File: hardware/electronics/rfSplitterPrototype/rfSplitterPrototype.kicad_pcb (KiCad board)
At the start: 4 copper layers, 40 x 40 mm, 43 parts, among them J1 PRPC002SBAN-M71RC, U1 TPS7A16A-Q1, U2 PMA2-162LNA+, U3 QCN-19D+

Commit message: worked on RF splitter
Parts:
- removed J1: PRPC002SBAN-M71RC, lib_fp:conn_01x02_254_right_angle
- added C10: 100pF, lib_fp:GCM0402, F.Cu at (141.0, 92.6)
- added C11: 100nF, lib_fp:GCM0402, F.Cu at (141.0, 93.8)
- added C13: 470pF, lib_fp:GCM0402, F.Cu at (142.2, 90.0)
- added J2: VAL, lib_fp:conn_01x03_254_right_angle, F.Cu at (153.7, 100.0)
- added L2: 68nH, lib_fp:L_0402, F.Cu at (140.5, 90.5)
- added NT1: NetTie, lib_fp:NetTie-2_SMD_Pad1.0mm, F.Cu at (131.2, 97.0)
- added TP12: ~, lib_fp:TP_2mm, F.Cu at (144.1, 92.6)
- TP9: value RCWCTE -> ~; footprint lib_fp:TP_RCW -> lib_fp:TP_2mm
- moved TP1 9.86 mm to (141.0, 106.4), turned to 0 degrees
- moved TP9 5.94 mm to (140.5, 87.2), turned to 0 degrees
- moved C14 3.35 mm to (144.3, 90.0)
- moved TP6 3.35 mm to (143.8, 87.2)
- moved TP7 3.30 mm to (146.3, 87.2)
- moved C12 3.10 mm to (151.1, 91.5)
- moved C15 3.10 mm to (156.0, 90.0)
- moved C16 3.10 mm to (146.6, 92.2)
- moved C7 3.10 mm to (155.9, 92.4)
- moved C8 3.10 mm to (155.9, 93.8)
- moved C9 3.10 mm to (153.5, 93.8)
- moved L1 3.10 mm to (154.0, 90.5)
- moved L3 3.10 mm to (146.1, 90.5)
- moved R4 3.10 mm to (153.5, 92.4)
- moved R5 3.10 mm to (152.5, 90.5)
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- renumbered C10 to C12, C11 to C14, C12 to C15, C13 to C16, L2 to L3, TP2 to TP1, TP1 to TP2
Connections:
- C14 pad 1: /GNSS_RF-IN -> Net-(C13-Pad2)
- TP6 pad 1: /GNSS_RF-IN -> Net-(C13-Pad2)
- TP9 pad 1: /LNA_RF-GND -> /GNSS_RF-IN
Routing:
- net +3V3: track 0.00 -> 55.5 mm, vias 0 -> 1
- net Net-(C13-Pad2): track 0.00 -> 3.90 mm
- net /RF-SPLIT_SUM: track 4.27 -> 6.17 mm
- net /LNA_RF-OUT: track 7.30 -> 9.08 mm
- net /GNSS_RF-IN: track 8.30 -> 9.55 mm
- net VSS: vias 9 -> 11
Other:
- board text added: "+3V3"
- board text added: "3V3"
- board text added: "5V0"
- board text added: "C14"
- board text removed: "+5V0"
- board text removed: "RF-GND"

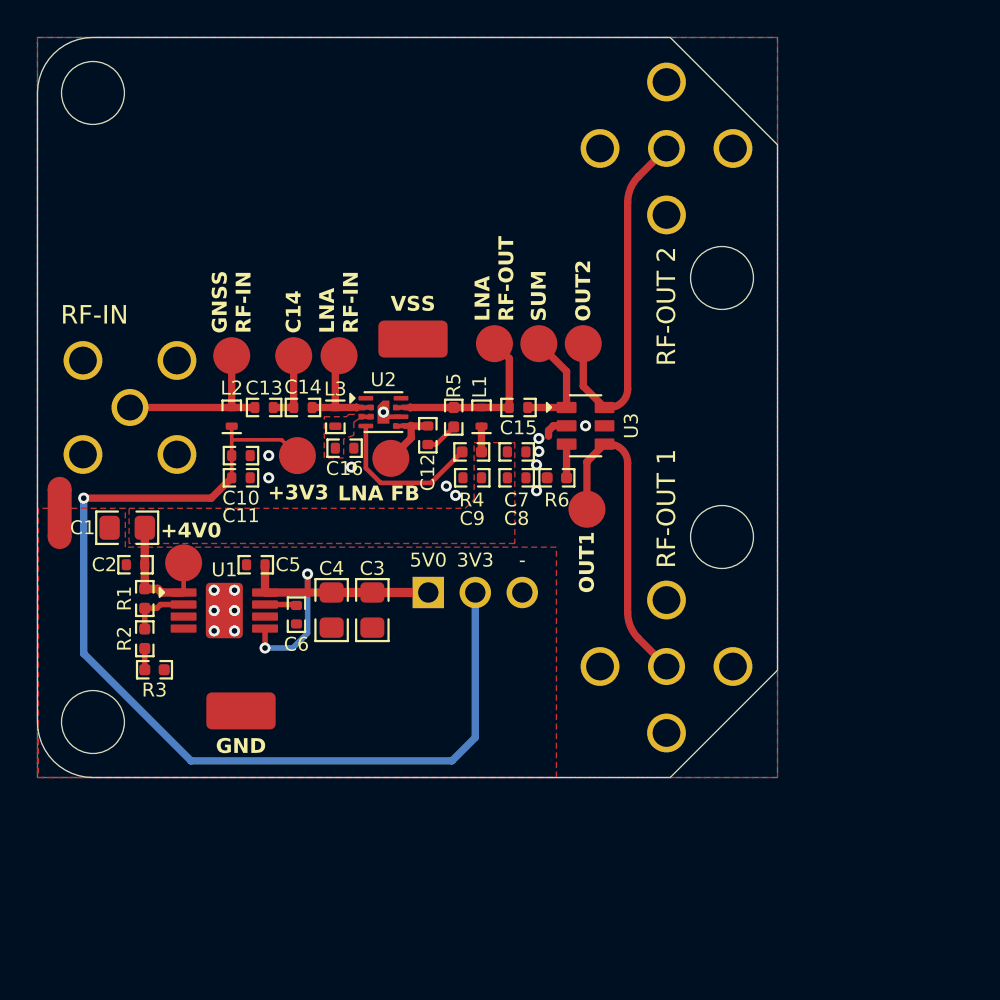
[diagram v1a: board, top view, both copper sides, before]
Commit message: updated with new LNA
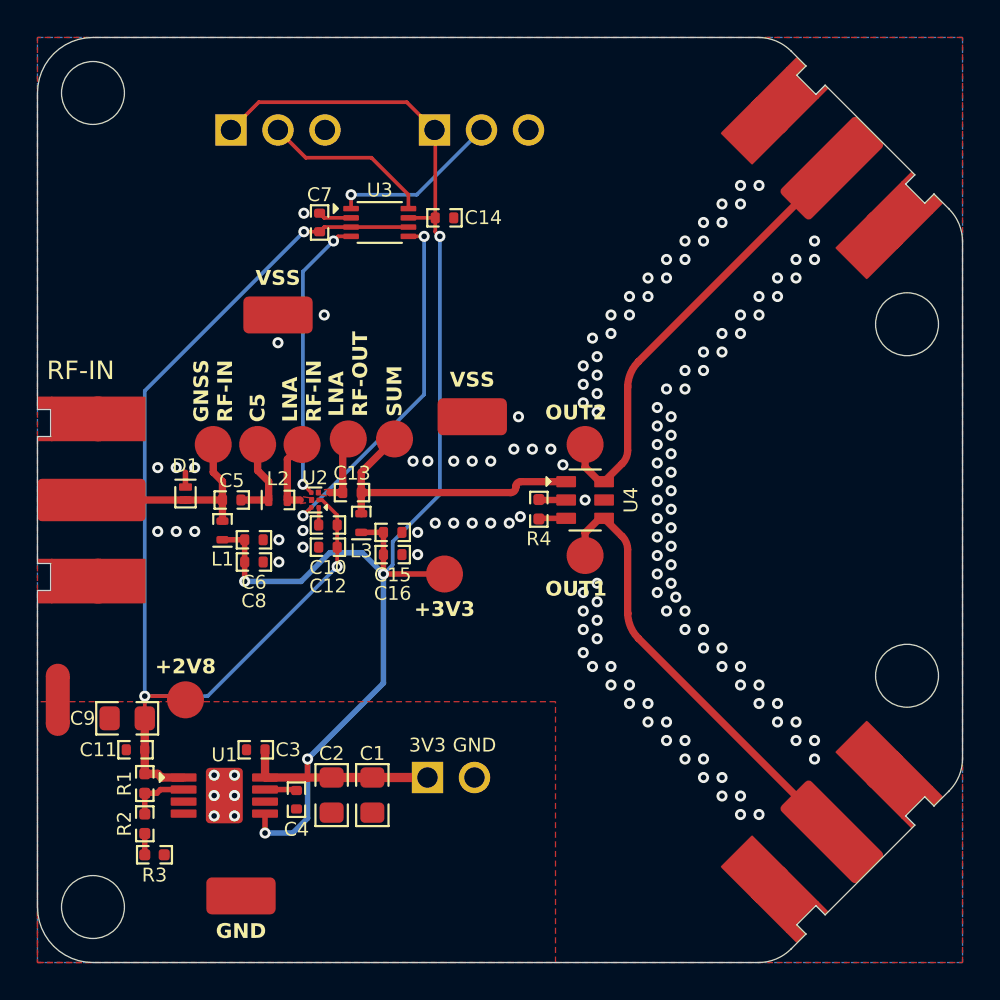
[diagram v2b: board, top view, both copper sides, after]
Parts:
- removed the C8 at (155.9, 93.8)
- removed the C9 at (153.5, 93.8)
- removed the L1 at (154.0, 90.5)
- removed the R4 at (153.5, 92.4)
- removed R5: 267R, lib_fp:CRCW0402
- removed the TP2 at (137.9, 98.4)
- removed the TP3 at (149.1, 92.8)
- removed the TP4 at (154.7, 86.5)
- removed the TP7 at (146.3, 87.2)
- removed the TP8 at (157.1, 86.5)
- added C10: 68pF, lib_fp:GCM0402, F.Cu at (145.7, 96.3)
- added C13: 470pF, lib_fp:GCM0402, F.Cu at (147.0, 94.6)
- added D1: PTVS4V5D1BLYL, lib_fp:SOD882, F.Cu at (138.0, 94.7)
- added J1: VAL, lib_fp:conn_01x02_254_right_angle, F.Cu at (152.3, 110.0)
- added J3: VAL, lib_fp:conn_01x03_254, F.Cu at (154.0, 75.0)
- added L2: 11nH, lib_fp:L_0402, F.Cu at (143.0, 95.0)
- added TP11: RCWCTE, lib_fp:TP_RCW, F.Cu at (143.0, 85.0)
- added TP12: ~, lib_fp:TP_2mm, F.Cu at (138.0, 105.8)
- added TP5: ~, lib_fp:TP_2mm, F.Cu at (144.3, 92.0)
- added TP6: ~, lib_fp:TP_2mm, F.Cu at (149.3, 91.7)
- added TP9: ~, lib_fp:TP_2mm, F.Cu at (146.8, 91.7)
- added U3: TXS0102-Q1, lib_fp:VSSOP50P310X90-8, F.Cu at (148.5, 80.0)
- AE1, AE2, AE3: footprint lib_fp:CONSMA002-G -> lib_fp:0732511153
- C12: value 5.6pF -> 100nF
- C14: value 9.1pF -> 100nF
- C16: value 100pF -> 100nF
- J2: footprint lib_fp:conn_01x03_254_right_angle -> lib_fp:conn_01x03_254
- L3: value 6.8nH -> 68nH
- R1: value 340K -> 220K
- R4: renamed from R6; value 49R9 -> 50R
- U2: value PMA2-162LNA+ -> BGA525N6; footprint lib_fp:TFDFN200X200X100-8 -> lib_fp:XDFN110X70X37-6
- moved J2 27.2 mm to (143.0, 75.0)
- moved C7 16.3 mm to (145.2, 80.0), turned to 90 degrees
- moved AE2 15.6 mm to (175.0, 115.0), turned to 45 degrees
- moved C14 12.8 mm to (152.0, 79.8)
- moved MH4 12.5 mm to (177.0, 104.5)
- moved AE3 11.0 mm to (175.0, 75.0), turned to 135 degrees
- moved MH2 10.3 mm to (177.0, 85.5)
- moved C9 10.3 mm to (134.8, 106.8)
- moved TP3 10.2 mm to (152.0, 99.0)
- moved NT1 10.1 mm to (131.1, 107.1)
- moved C1 10.0 mm to (148.1, 111.0)
- moved C11 10.0 mm to (135.3, 108.5)
- moved C2 10.0 mm to (145.9, 111.0)
- moved C3 10.0 mm to (141.8, 108.5)
- moved C4 10.0 mm to (144.0, 111.2)
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- renumbered C3 to C1, C2 to C11, C4 to C2, C5 to C3, C6 to C4, C13 to C5, C10 to C6, C11 to C8, C1 to C9, L2 to L1, MH3 to MH2, MH2 to MH3, TP9 to TP2, TP12 to TP3, TP6 to TP4, TP5 to TP7, TP11 to TP8, U3 to U4
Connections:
- C1 pad 1: VIN -> +3V3
- C11 pad 1: +4V0 -> +2V8
- C12 pad 1: /LNA_FB -> +2V8
- C12 pad 2: Net-(C12-Pad2) -> VSS
- C14 pad 1: Net-(C13-Pad2) -> +3V3
- C14 pad 2: /LNA_RF-IN -> VSS
- C15 pad 1: /LNA_RF-OUT -> +3V3
- C15 pad 2: /RF-SPLIT_SUM -> VSS
- C16 pad 1: /LNA_RF-GND -> +3V3
- C2 pad 1: VIN -> +3V3
- C3 pad 1: VIN -> +3V3
- C5 pad 2: Net-(C13-Pad2) -> Net-(C5-Pad2)
- C7 pad 1: +4V0 -> +2V8
- C9 pad 1: +4V0 -> +2V8
- J2 pad 1: VIN -> +3V3
- J2 pad 2: +3V3 -> /CTRL1_3V3
- J2 pad 3: GND -> VSS
- L3 pad 1: /LNA_RF-IN -> +3V3
- L3 pad 2: /LNA_RF-GND -> /RF-SPLIT_SUM
- R1 pad 1: +4V0 -> +2V8
- TP4 pad 1: Net-(C13-Pad2) -> Net-(C5-Pad2)
- U1 pad 1: +4V0 -> +2V8
- U1 pad 5: VIN -> +3V3
- U1 pad 8: VIN -> +3V3
- U2 pad 2: /LNA_RF-IN -> +2V8
- U2 pad 3: /LNA_RF-GND -> Net-(U2-AO)
- U2 pad 4: /LNA_BIAS -> /CTRL2
- U2 pad 5: /LNA_FB -> /LNA_RF-IN
- U2 pad 6: VSS -> /CTRL1
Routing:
- net +2V8: track 0.00 -> 60.5 mm, vias 0 -> 3
- net +3V3: track 55.5 -> 87.8 mm, vias 1 -> 5
- net /CTRL1: track 0.00 -> 19.3 mm, vias 0 -> 2
- net VIN: track 18.2 -> 0.00 mm, vias 2 -> 0
- net /CTRL2: track 0.00 -> 15.5 mm, vias 0 -> 2
- net /RF-SPLIT_SUM: track 6.17 -> 16.2 mm
- net /CTRL2_3V3: track 0.00 -> 9.25 mm, vias 0 -> 1
- net /CTRL1_3V3: track 0.00 -> 9.25 mm
- net /LNA_RF-OUT: track 9.08 -> 0.00 mm
- net /LNA_BIAS: track 8.50 -> 0.00 mm
- net +4V0: track 8.47 -> 0.00 mm
- net /GNSS_CONN1: track 17.2 -> 24.6 mm
- net /GNSS_CONN2: track 19.2 -> 24.6 mm
- net Net-(C5-Pad2): track 0.00 -> 4.74 mm
- net Net-(C13-Pad2): track 3.90 -> 0.00 mm
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- added copper zone on F.Cu, net Net-(U2-AO)
- removed copper zone on F.Cu, net +4V0
- removed copper zone on F.Cu, net /LNA_FB
- removed copper zone on F.Cu, net /LNA_RF-GND
- removed copper zone on F.Cu, net /LNA_RF-OUT
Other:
- board size 40 x 40 mm -> 50 x 50 mm
- rule pad_to_mask_clearance: 0 -> 0.0762
- board text added: "+2V8"
- board text added: "C5"
- board text removed: "+4V0"
- board text removed: "-"
- board text removed: "5V0"
- board text removed: "C14"
- board text removed: "LNA FB"
- board text removed: "RF-OUT 1"
- board text removed: "RF-OUT 2"
